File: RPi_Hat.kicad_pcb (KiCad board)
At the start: 2 copper layers, 65 x 56 mm, 23 parts, among them J1 CONN_02X19, J2 RPi_GPIO, J3 CONN_02X06, J4 CONN_02X06, J5 CONN_02X06, J6 CONN_02X10, J7 CONN_02X10, J8 CONN_02X10, U1 DS1307Z+, U2 CAT24C32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

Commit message: cleanup and add RX/TX header
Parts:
- removed C1: CAP, Capacitors_SMD:C_0805_HandSoldering
- removed R1: R, Resistors_SMD:R_0805_HandSoldering
- added J9: CONN_01X04, Pin_Headers:Pin_Header_Straight_1x04_Pitch2.54mm, F.Cu at (55.8, 15.5)
- moved Y1 14.5 mm to (25.1, 31.9)
- moved R2 10.6 mm to (51.5, 12.6)
- moved R3 10.3 mm to (51.5, 10.4)
- moved R4 10.1 mm to (51.5, 8.31)
- moved JP1 10.0 mm to (59.5, 11.3), turned to 90 degrees
- moved C2 9.74 mm to (35.6, 8.15)
- moved U2 8.87 mm to (43.6, 10.1)
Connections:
- net Pin10 renamed RX
- net Pin8 renamed TX
- J3 pad 1: Net-(J3-Pad1) -> 3.3V
- J5 pad 2: Net-(J5-Pad2) -> GND
- J6 pad 2: Net-(J6-Pad2) -> GND
- J8 pad 1: Net-(J8-Pad1) -> 3.3V
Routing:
- net GND: track 423.3 -> 530.6 mm, vias 2 -> 0
- net TX: track 17.1 -> 84.6 mm
- net RX: track 20.7 -> 80.2 mm
- net Net-(U1-Pad2): track 19.9 -> 5.36 mm
- net Net-(U1-Pad1): track 17.5 -> 4.55 mm
- net ID_SD: track 22.6 -> 10.2 mm
- net ID_SC: track 32.6 -> 20.3 mm
- net Net-(U1-Pad7): track 6.64 -> 0.56 mm
- net 3.3V: track 167.0 -> 171.6 mm
- net Net-(JP1-Pad1): track 15.7 -> 20.0 mm
- net Net-(C1-Pad1): track 4.08 -> 0.00 mm
- net Pin40: track 72.0 -> 72.7 mm

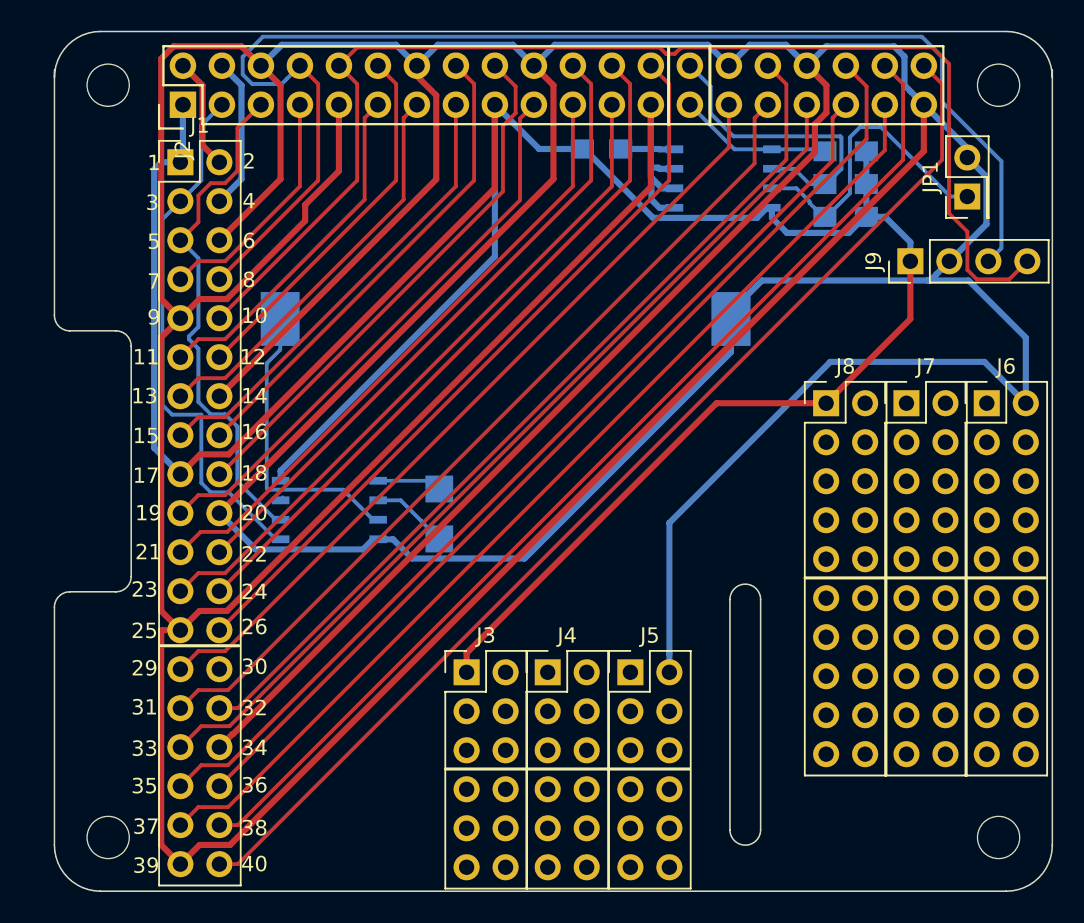
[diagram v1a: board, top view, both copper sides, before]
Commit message: support MCP7940N as well as ds1338/ds1340
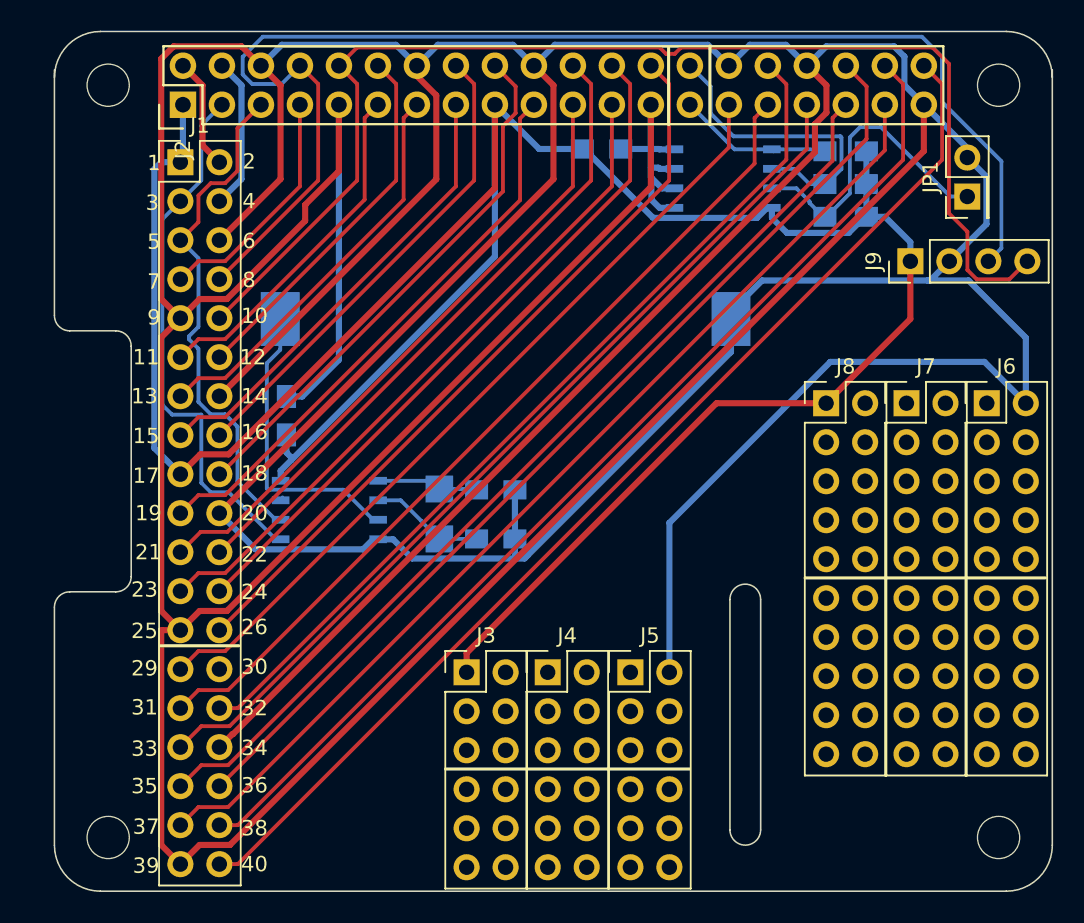
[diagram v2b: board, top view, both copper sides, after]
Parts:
- added C1: C, Capacitors_SMD:C_0805_HandSoldering, B.Cu at (28.7, 30.4)
- added C3: C, Capacitors_SMD:C_0805_HandSoldering, B.Cu at (28.7, 33.6)
- added C4: C, Capacitors_SMD:C_0805_HandSoldering, B.Cu at (15.1, 25.5)
- turned Y1 to 90 degrees
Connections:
- U1 pad 1: Net-(U1-Pad1) -> Net-(C1-Pad2)
- U1 pad 2: Net-(U1-Pad2) -> Net-(C3-Pad2)
- Y1 pad 1: Net-(U1-Pad1) -> Net-(C3-Pad2)
- Y1 pad 2: Net-(U1-Pad2) -> Net-(C1-Pad2)
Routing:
- net GND: track 530.6 -> 556.7 mm
- net Net-(C3-Pad2): track 0.00 -> 7.79 mm
- net Net-(C1-Pad2): track 0.00 -> 6.97 mm
- net Net-(U1-Pad2): track 5.36 -> 0.00 mm
- net Net-(U1-Pad1): track 4.55 -> 0.00 mm
- net 3.3V: track 171.6 -> 173.4 mm
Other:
- rule via_min_size: 0.4 -> 0.6

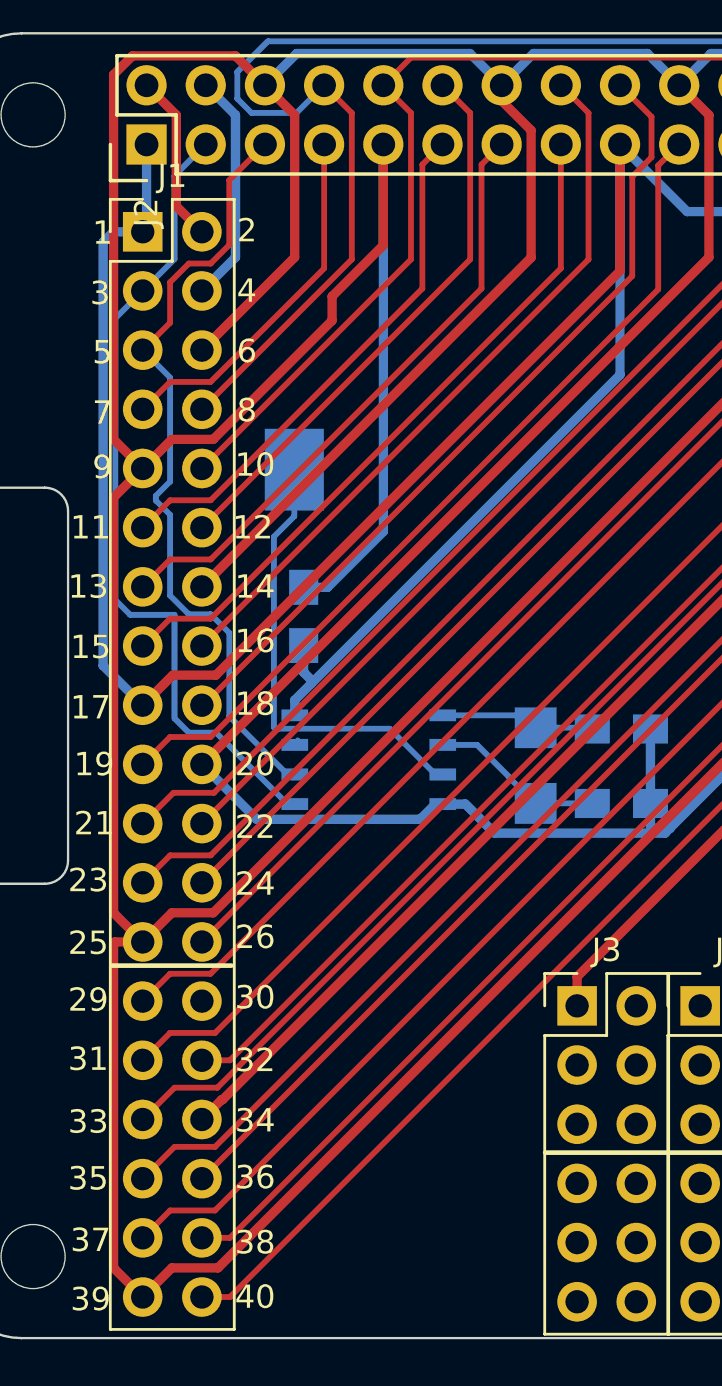
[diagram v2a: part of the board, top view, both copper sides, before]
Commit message: add room for an rgb led
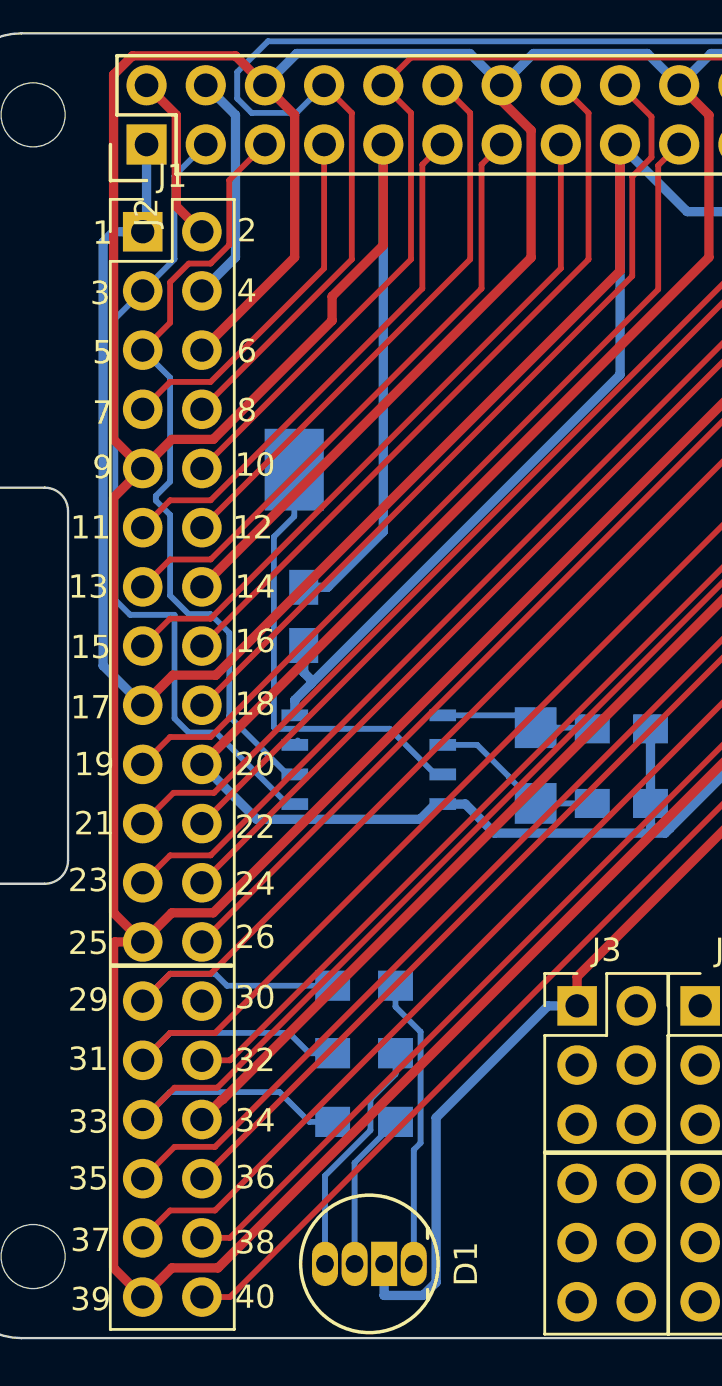
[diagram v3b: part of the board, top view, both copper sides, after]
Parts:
- added D1: LED_RABG, LEDs:LED-RGB-5MM_Common_Cathode, F.Cu at (19.8, 53.3)
- added R1: R, Resistors_SMD:R_0805_HandSoldering, B.Cu at (17.7, 41.4)
- added R5: R, Resistors_SMD:R_0805_HandSoldering, B.Cu at (17.7, 44.3)
- added R6: R, Resistors_SMD:R_0805_HandSoldering, B.Cu at (17.7, 47.2)
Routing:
- net 3.3V: track 173.4 -> 192.3 mm
- net Net-(D1-Pad1): track 0.00 -> 12.5 mm
- net Net-(D1-Pad4): track 0.00 -> 10.4 mm
- net Pin33: track 59.8 -> 69.0 mm
- net Pin31: track 56.3 -> 65.3 mm
- net Pin29: track 52.6 -> 61.4 mm
- net Net-(D1-Pad3): track 0.00 -> 6.93 mm

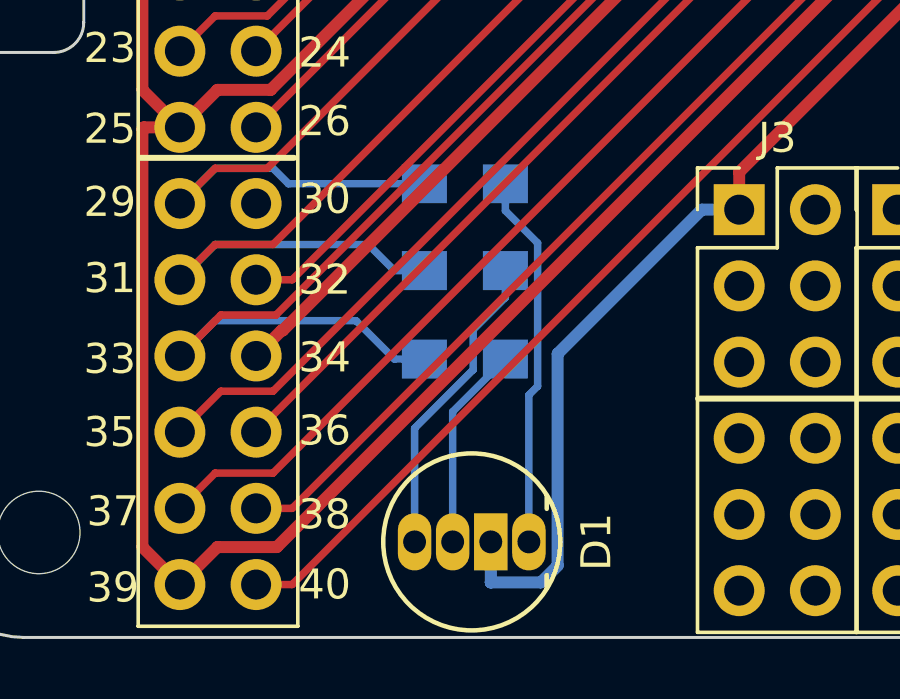
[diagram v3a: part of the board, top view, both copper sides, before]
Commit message: use connector footprint for LED as the standard one violated the DRC
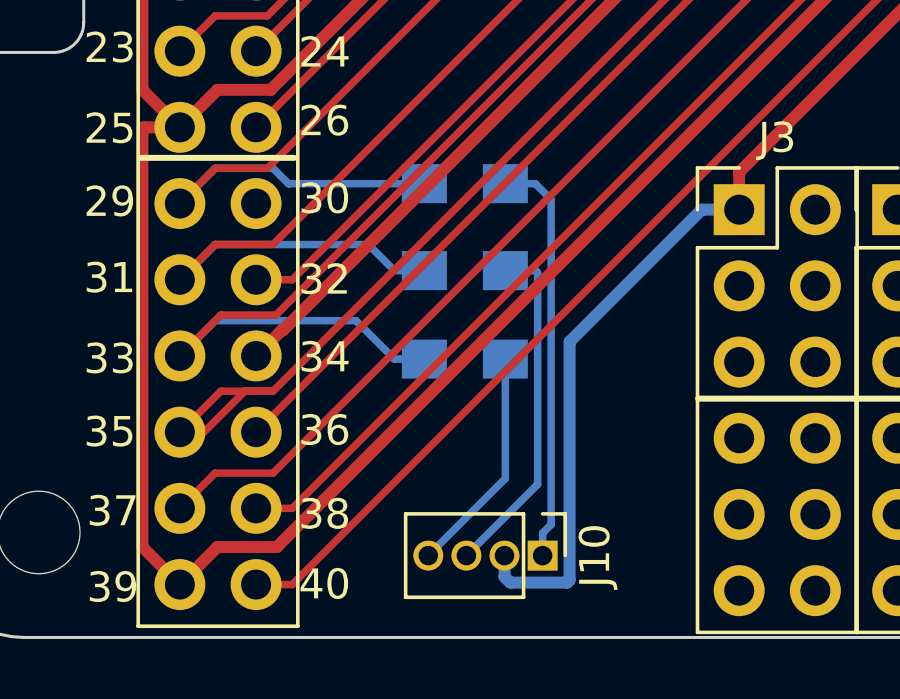
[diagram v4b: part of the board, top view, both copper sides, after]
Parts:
- removed D1: LED_RABG, LEDs:LED-RGB-5MM_Common_Cathode
- added J10: CONN_01X04, Pin_Headers:Pin_Header_Straight_1x04_Pitch1.27mm, F.Cu at (20.3, 53.8)
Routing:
- net Pin35: track 63.4 -> 66.6 mm
- net Net-(J10-Pad1): track 12.5 -> 13.8 mm
- net Net-(J10-Pad3): track 10.4 -> 11.6 mm
- net Net-(J10-Pad4): track 6.93 -> 7.72 mm
- net 3.3V: track 192.3 -> 191.8 mm

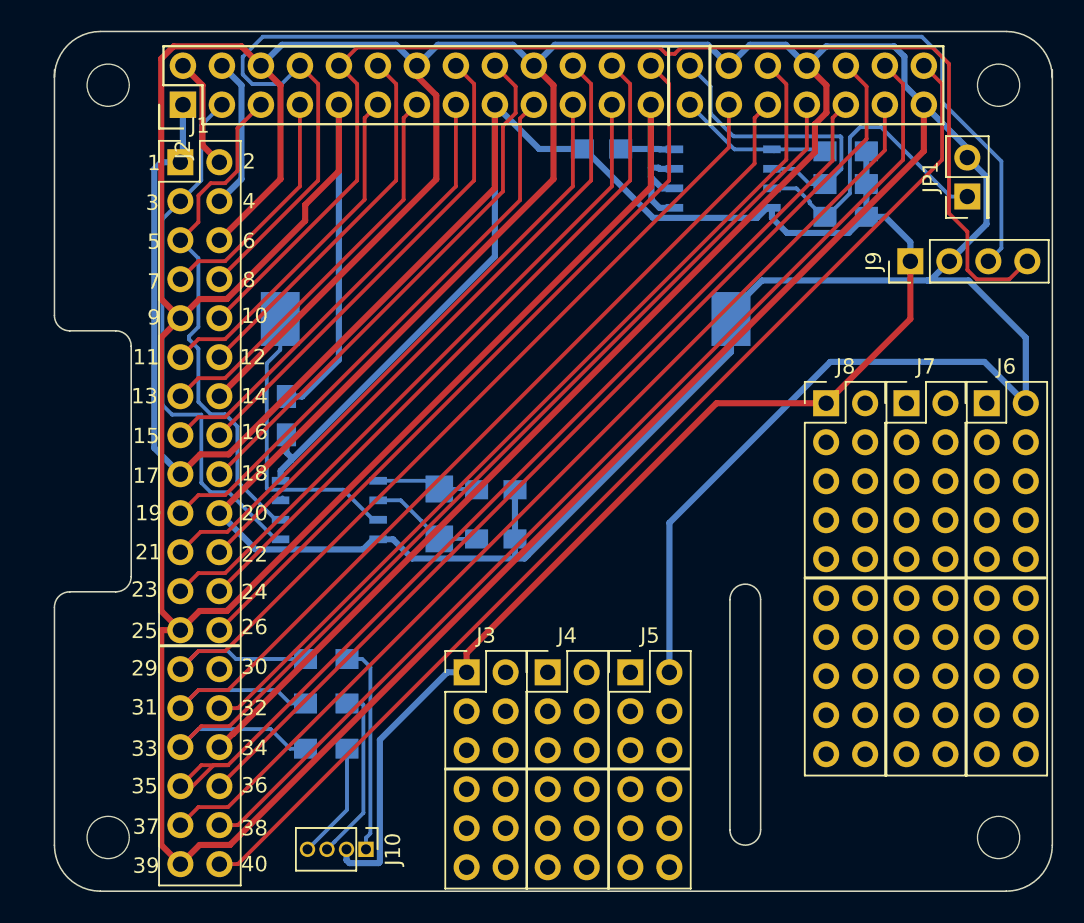
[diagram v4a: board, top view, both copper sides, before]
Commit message: move LED to front and make sure there is enough clearance between components
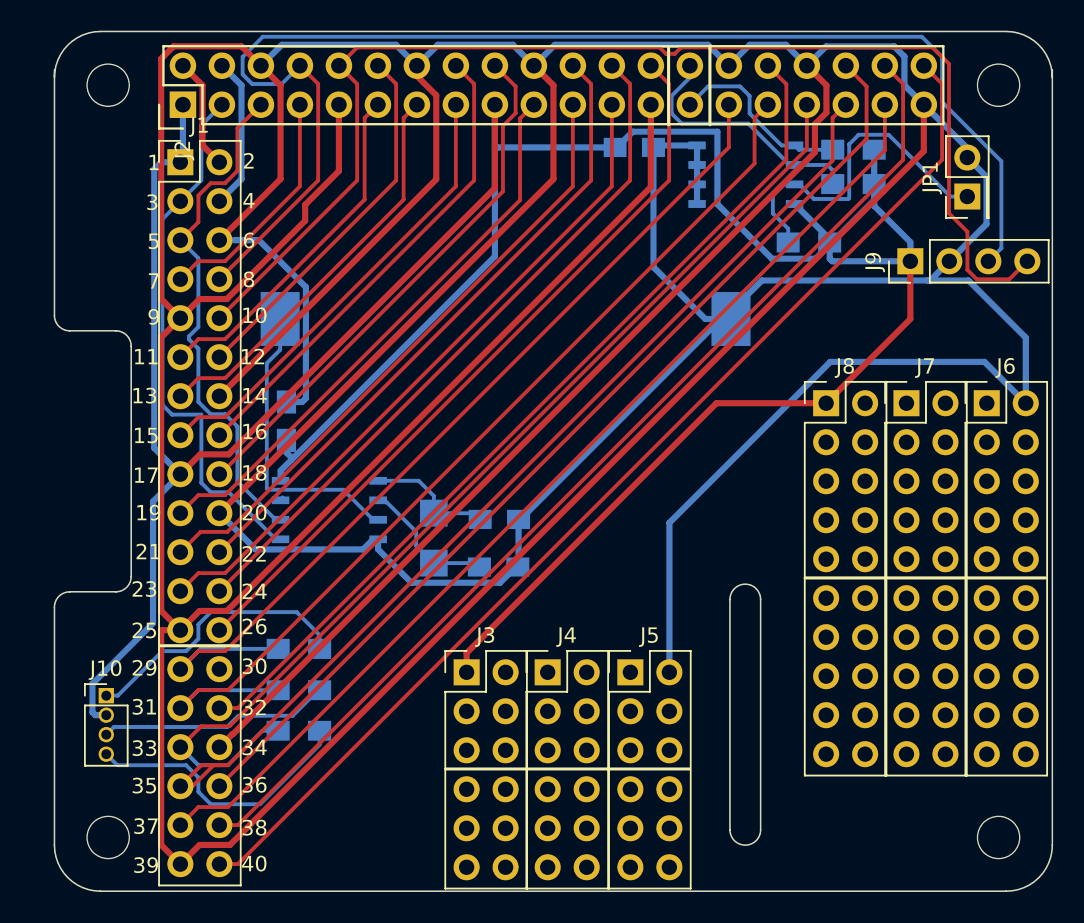
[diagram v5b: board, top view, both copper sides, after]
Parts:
- moved J10 19.7 mm to (3.38, 43.8), turned to 0 degrees
- moved R2 2.92 mm to (49.1, 14.2)
- moved C2 2.14 mm to (37.8, 8.05)
- moved R6 2.13 mm to (15.9, 46.1)
- moved R5 1.98 mm to (15.9, 43.4)
- moved C1 1.94 mm to (29.0, 32.3)
- moved R1 1.90 mm to (15.9, 40.7)
- moved C3 1.84 mm to (28.9, 35.4)
- moved Y1 1.61 mm to (24.7, 33.5)
- moved U2 1.49 mm to (45.0, 9.83)
- moved R4 0.52 mm to (52.0, 8.20)
- moved R3 0.51 mm to (52.0, 10.4)
- moved C4 0.36 mm to (15.1, 25.9)
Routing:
- net 3.3V: track 191.8 -> 204.9 mm
- net Net-(J10-Pad4): track 7.72 -> 18.3 mm
- net Net-(J10-Pad1): track 13.8 -> 18.2 mm
- net ID_SC: track 20.3 -> 16.8 mm
- net Net-(J10-Pad3): track 11.6 -> 15.1 mm
- net Net-(JP1-Pad1): track 20.0 -> 22.4 mm
- net GND: track 556.7 -> 554.4 mm
- net Pin31: track 65.3 -> 63.1 mm
- net ID_SD: track 10.2 -> 12.2 mm
- net Pin29: track 61.4 -> 59.5 mm
- net Net-(C1-Pad2): track 6.97 -> 8.69 mm
- net Net-(C3-Pad2): track 7.79 -> 9.25 mm
- net Pin33: track 69.0 -> 67.6 mm
